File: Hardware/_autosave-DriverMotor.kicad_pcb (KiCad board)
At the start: 2 copper layers, 103 parts, among them J1 Conn_02x03_Odd_Even, J10 Screw_Terminal_01x04, J11 Screw_Terminal_01x04, J12 Screw_Terminal_01x04, J13 Screw_Terminal_01x02, J2 Screw_Terminal_01x02, J3 Conn_02x04_Counter_Clockwise, J4 Screw_Terminal_01x04, J5 Screw_Terminal_01x03, J6 Screw_Terminal_01x03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

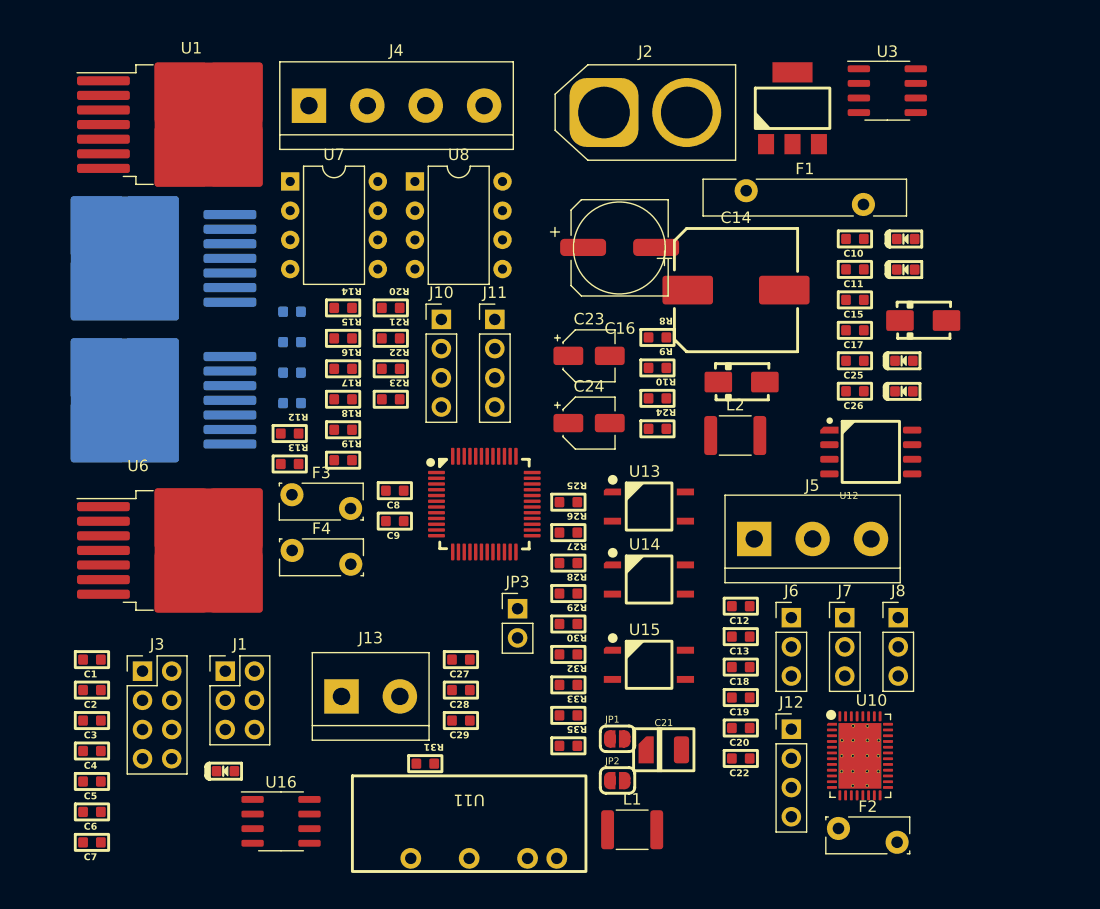
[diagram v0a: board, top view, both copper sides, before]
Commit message: Update schematic part2
Vẽ bus dành cho khối BLDC
Đóng khối chức năng cho sheet MCT8316
Tạo sheet nguồn cho các mạch nguồn Buck DCDC, LDO LD1117, BS0505
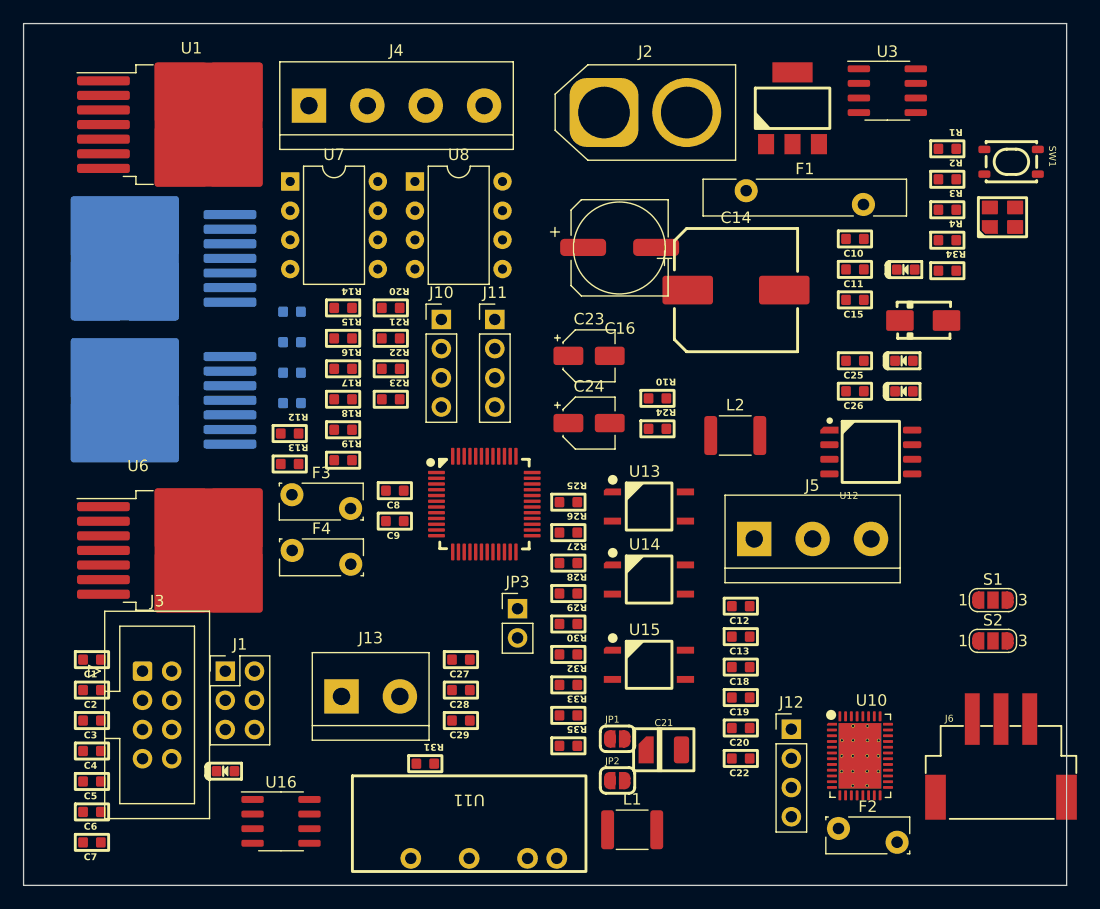
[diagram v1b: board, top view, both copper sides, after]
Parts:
- removed C17: 3.3nF, IVS_FOOTPRINTS:C_0603
- removed D3: SS54, IVS_FOOTPRINTS:Package-Diode-D_SMA
- removed D4: LED, IVS_FOOTPRINTS:LED_0603
- removed J7, J8: Conn_01x03_Pin, Connector_PinHeader_2.54mm:PinHeader_1x03_P2.54mm_Vertical
- removed R8: 1K, IVS_FOOTPRINTS:R_0603
- removed R9: 3K1, IVS_FOOTPRINTS:R_0603
- added R1: 10k, IVS_FOOTPRINTS:R_0603, F.Cu at (217.7, 99.7)
- added R2: 10k, IVS_FOOTPRINTS:R_0603, F.Cu at (217.7, 102.3)
- added R3: 10K, IVS_FOOTPRINTS:R_0603, F.Cu at (217.7, 105.0)
- added R34: 2K2, IVS_FOOTPRINTS:R_0603, F.Cu at (217.7, 110.3)
- added R4: 1M, IVS_FOOTPRINTS:R_0603, F.Cu at (217.7, 107.6)
- added S1: SolderJump3P, Jumper:SolderJumper-3_P1.3mm_Open_RoundedPad1.0x1.5mm_NumberLabels, F.Cu at (221.7, 138.9)
- added S2: SolderJump3P, Jumper:SolderJumper-3_P1.3mm_Open_RoundedPad1.0x1.5mm_NumberLabels, F.Cu at (221.7, 142.5)
- added SW1: SW_Push, IVS_FOOTPRINTS:ButtonPush-Vert-SMD-4P-SPST_PTS810, F.Cu at (223.3, 100.8)
- added Y1: 8Mhz, IVS_FOOTPRINTS:Crystal-SMD-4P-3.2x2.6mm-3225, F.Cu at (222.5, 105.6)
- J3: footprint Connector_PinHeader_2.54mm:PinHeader_2x04_P2.54mm_Vertical -> Connector_IDC:IDC-Header_2x04_P2.54mm_Vertical
- J6: footprint Connector_PinHeader_2.54mm:PinHeader_1x03_P2.54mm_Vertical -> IVS_FOOTPRINTS:Conn-Horz-SMD-3P-2.54mm-S3B_XH_SM4_TB
- moved J6 22.4 mm to (222.2, 153.7)
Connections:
- J12 pad 1: /MCT8316/MCU_PWM_BLDC -> /MCT8316/MCT.PWM
- J12 pad 3: /MCT8316/MCU_DIR -> /MCT8316/MCT.DIR
- J12 pad 4: /MCT8316/MCU_BRAKE -> /MCT8316/MCT.BRAKE
- R25 pad 1: /MCT8316/MCU_PWM_BLDC -> /MCT8316/MCT.PWM
- R33 pad 2: /MCT8316/MCU_FG -> /MCT8316/MCT.FG
- U10 pad 41: (no net) -> GNDD
- U12 pad 2: /MCT8316/MCU_FG -> /MCT8316/MCT.FG
- U13 pad 4: /MCT8316/MCU_FAULT -> /MCT8316/MCT.FAULT
- U14 pad 1: /MCT8316/MCU_BRAKE -> /MCT8316/MCT.BRAKE
- U15 pad 1: /MCT8316/MCU_DIR -> /MCT8316/MCT.DIR
- U16 pad 1: /TJA1050/CAN_TX -> /STM32F103/CANTX
- U16 pad 4: /TJA1050/CAN_RX -> /STM32F103/CANRX
- U5 pad 25: /STM32F103/MCU_FG -> /MCT8316/MCT.FG
- U5 pad 26: /STM32F103/MCU_FAULT -> /MCT8316/MCT.FAULT
- U5 pad 27: /STM32F103/MCU_BRAKE -> /MCT8316/MCT.BRAKE
- U5 pad 28: /STM32F103/MCU_DIR -> /MCT8316/MCT.DIR
- U5 pad 41: /STM32F103/MCU_PWM_BLDC -> /MCT8316/MCT.PWM
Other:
- board outline added: 90.8 x 75 mm
